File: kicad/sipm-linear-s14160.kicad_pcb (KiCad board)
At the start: 4 copper layers, 113.2 x 74.6 mm, 221 parts, among them J1 SSQ-103-01-G-D, J10 Conn_Coaxial, J11 Conn_Coaxial, J12 Conn_Coaxial, J13 Conn_Coaxial, J14 Conn_Coaxial, J15 Conn_Coaxial, J16 Conn_Coaxial, J17 Conn_Coaxial, J18 SSQ-103-01-G-D, J2 Conn_Coaxial, J3 Conn_Coaxial, J4 Conn_Coaxial, J5 Conn_Coaxial, J6 Conn_Coaxial, J7 Conn_Coaxial, J8 Conn_Coaxial, J9 Conn_Coaxial, U1 OPA847IDBVT, U10 OPA847IDBVT, U11 OPA847IDBVT, U12 OPA847IDBVT, U13 OPA847IDBVT, U14 OPA847IDBVT, U15 OPA847IDBVT, U16 OPA847IDBVT, U17 OPA847IDBVT, U2 S15643, U3 OPA847IDBVT, U4 OPA847IDBVT, U5 OPA847IDBVT, U6 OPA847IDBVT, U7 OPA847IDBVT, U8 OPA847IDBVT, U9 OPA847IDBVT

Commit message: Rename to reflect that we are using the s14160 elements in the array
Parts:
- moved J3 9.34 mm to (147.8, 77.2)
- moved J15 9.28 mm to (147.8, 130.8)
- moved J5 9.24 mm to (147.8, 87.9)
- moved J11 9.23 mm to (147.8, 120.1)
- moved J7 9.21 mm to (147.8, 98.6)
- moved J9 9.20 mm to (147.8, 109.4)
- moved J13 7.70 mm to (168.4, 74.6)
- moved C14 7.46 mm to (183.7, 104.2), turned to 0 degrees
- moved J18 6.58 mm to (178.4, 130.9)
- moved J17 6.05 mm to (168.2, 130.2)
- moved C40 5.16 mm to (183.7, 97.8), turned to 0 degrees
- moved J16 5.00 mm to (200.4, 130.4)
- moved L12 3.01 mm to (180.6, 89.8)
- moved J10 2.50 mm to (220.3, 119.1)
- moved J14 2.50 mm to (220.3, 108.6)
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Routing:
- added copper zone on In2.Cu, net /VBias2
- added copper zone on In2.Cu, net /VSSA2
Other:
- board size 113.2 x 74.6 mm -> 90.8 x 68.9 mm

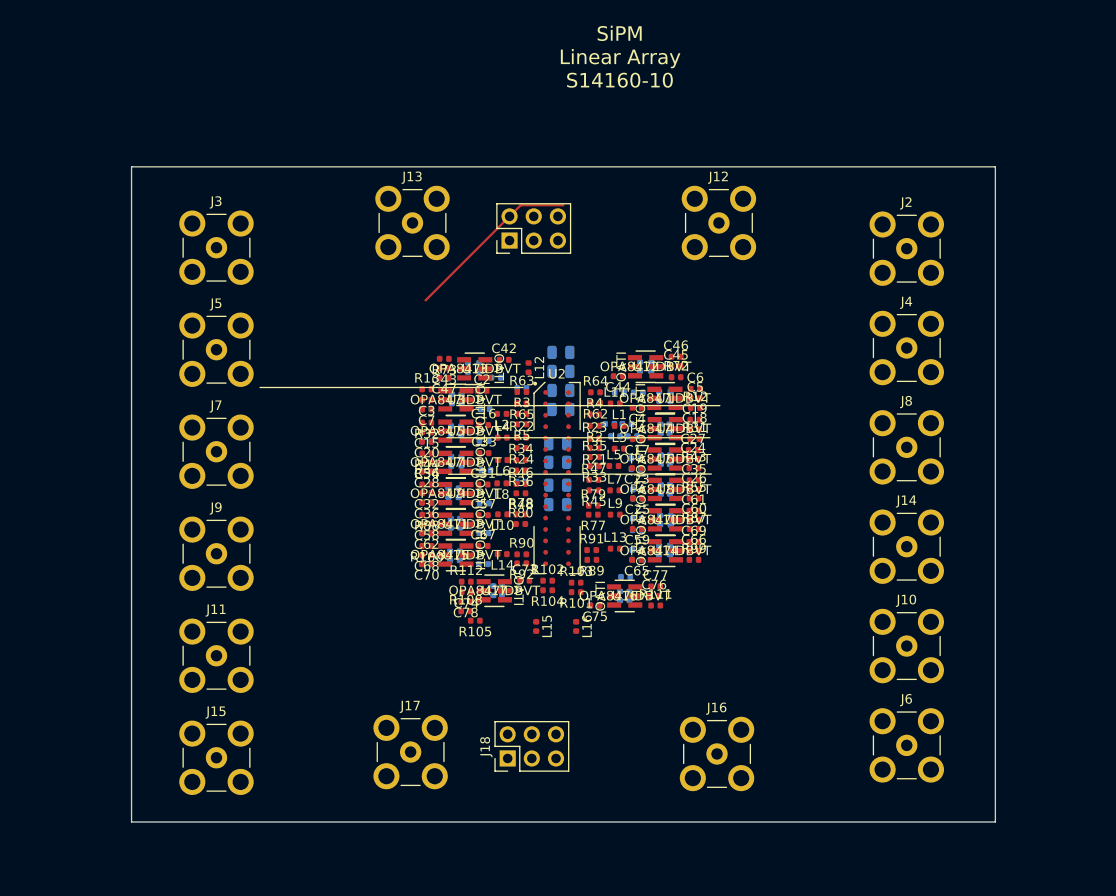
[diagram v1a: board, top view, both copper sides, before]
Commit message: Check in before removing feedback cap
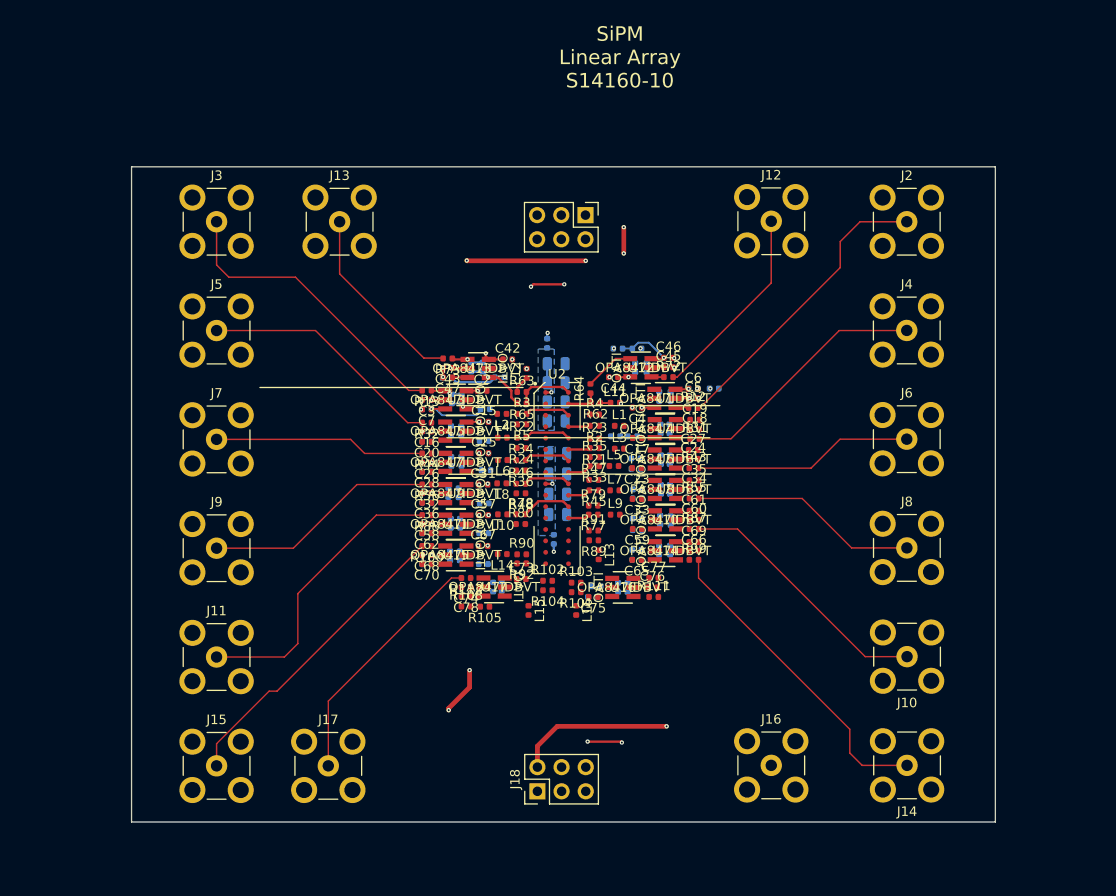
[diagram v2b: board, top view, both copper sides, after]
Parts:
- moved J6 32.2 mm to (220.3, 97.3)
- moved C34 28.2 mm to (198.0, 102.6), turned to 0 degrees
- moved C26 28.2 mm to (169.9, 99.8), turned to 180 degrees
- moved J14 23.0 mm to (220.4, 131.6), turned to 180 degrees
- moved C25 16.8 mm to (175.9, 98.8), turned to 0 degrees
- moved C33 16.8 mm to (192.0, 103.6), turned to 180 degrees
- moved J8 10.6 mm to (220.3, 108.7)
- moved R7 9.90 mm to (200.1, 92.0)
- moved R8 9.53 mm to (197.9, 92.0), turned to 180 degrees
- moved J17 8.77 mm to (159.6, 131.7)
- moved J1 8.41 mm to (186.6, 73.8), turned to -90 degrees
- moved J13 7.66 mm to (160.7, 74.5)
- moved R59 6.94 mm to (183.2, 107.8), turned to 90 degrees
- moved C15 6.10 mm to (175.9, 95.5), turned to 0 degrees
- moved C16 6.01 mm to (169.9, 96.5), turned to 180 degrees
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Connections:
- C31 pad 1: /VSSA2 -> /VDDA2
- C32 pad 1: /VDDA2 -> /VSSA2
- C33 pad 1: /VSSA2 -> /VDDA2
- C34 pad 1: /VDDA2 -> /VSSA2
- C57 pad 1: /VSSA2 -> /VDDA2
- C58 pad 1: /VDDA2 -> /VSSA2
- C59 pad 1: /VSSA2 -> /VDDA2
- C60 pad 1: /VDDA2 -> /VSSA2
- C65 pad 1: /VSSA2 -> /VDDA2
- C66 pad 1: /VDDA2 -> /VSSA2
- C67 pad 1: /VSSA2 -> /VDDA2
- C68 pad 1: /VDDA2 -> /VSSA2
- C73 pad 1: /VSSA2 -> /VDDA2
- C74 pad 1: /VDDA2 -> /VSSA2
- C75 pad 1: /VSSA2 -> /VDDA2
- C76 pad 1: /VDDA2 -> /VSSA2
- J1 pad 1: +5V -> unconnected-(J1-Pad1)
- J18 pad 1: +5V -> unconnected-(J18-Pad1)
- J18 pad 4: (no net) -> /LINE2
- R105 pad 1: LINE -> /LINE2
- R106 pad 2: LINE -> /LINE2
- R49 pad 1: LINE -> /LINE2
- R50 pad 2: LINE -> /LINE2
- R81 pad 1: LINE -> /LINE2
- R82 pad 2: LINE -> /LINE2
- R93 pad 1: LINE -> /LINE2
- R94 pad 2: LINE -> /LINE2
- U1 pad 5: (no net) -> unconnected-(U1-Pad5)
- U10 pad 2: /VDDA2 -> /VSSA2
- U10 pad 5: (no net) -> unconnected-(U10-Pad5)
- U10 pad 6: /VSSA2 -> /VDDA2
- U11 pad 2: /VDDA2 -> /VSSA2
- U11 pad 5: (no net) -> unconnected-(U11-Pad5)
- U11 pad 6: /VSSA2 -> /VDDA2
- U12 pad 5: (no net) -> unconnected-(U12-Pad5)
- U13 pad 5: (no net) -> unconnected-(U13-Pad5)
- U14 pad 2: /VDDA2 -> /VSSA2
- U14 pad 5: (no net) -> unconnected-(U14-Pad5)
- U14 pad 6: /VSSA2 -> /VDDA2
- U15 pad 2: /VDDA2 -> /VSSA2
- U15 pad 5: (no net) -> unconnected-(U15-Pad5)
- U15 pad 6: /VSSA2 -> /VDDA2
- U16 pad 2: /VDDA2 -> /VSSA2
- U16 pad 5: (no net) -> unconnected-(U16-Pad5)
- U16 pad 6: /VSSA2 -> /VDDA2
- U17 pad 2: /VDDA2 -> /VSSA2
- U17 pad 5: (no net) -> unconnected-(U17-Pad5)
- U17 pad 6: /VSSA2 -> /VDDA2
- U2 pad 11: (no net) -> unconnected-(U2-Pad11)
- U2 pad 13: (no net) -> unconnected-(U2-Pad13)
- U2 pad 15: (no net) -> unconnected-(U2-Pad15)
- U2 pad 19: (no net) -> unconnected-(U2-Pad19)
- U2 pad 21: (no net) -> unconnected-(U2-Pad21)
- U2 pad 23: (no net) -> unconnected-(U2-Pad23)
- U2 pad 25: (no net) -> unconnected-(U2-Pad25)
- U2 pad 27: (no net) -> unconnected-(U2-Pad27)
- U2 pad 29: (no net) -> unconnected-(U2-Pad29)
- U2 pad 3: (no net) -> unconnected-(U2-Pad3)
- U2 pad 31: (no net) -> unconnected-(U2-Pad31)
- U2 pad 5: (no net) -> unconnected-(U2-Pad5)
- U2 pad 7: (no net) -> unconnected-(U2-Pad7)
- U2 pad 9: (no net) -> unconnected-(U2-Pad9)
- U3 pad 5: (no net) -> unconnected-(U3-Pad5)
- U4 pad 5: (no net) -> unconnected-(U4-Pad5)
- U5 pad 5: (no net) -> unconnected-(U5-Pad5)
- U6 pad 5: (no net) -> unconnected-(U6-Pad5)
- U7 pad 5: (no net) -> unconnected-(U7-Pad5)
- U8 pad 2: /VDDA2 -> /VSSA2
- U8 pad 5: (no net) -> unconnected-(U8-Pad5)
- U8 pad 6: /VSSA2 -> /VDDA2
- U9 pad 2: /VDDA2 -> /VSSA2
- U9 pad 5: (no net) -> unconnected-(U9-Pad5)
- U9 pad 6: /VSSA2 -> /VDDA2
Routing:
- net /VDDA2: track 0.00 -> 67.8 mm, vias 0 -> 5
- net /VSSA2: track 0.00 -> 57.7 mm, vias 0 -> 4
- net /LINE2: track 0.00 -> 46.6 mm, vias 0 -> 2
- net GND: track 34.6 -> 1.00 mm, vias 0 -> 24
- net Net-(J14-Pad1): track 0.00 -> 33.4 mm
- net Net-(J15-Pad1): track 0.00 -> 32.5 mm
- net Net-(J2-Pad1): track 0.00 -> 31.7 mm
- net Net-(J3-Pad1): track 0.00 -> 31.6 mm
- net Net-(J11-Pad1): track 0.00 -> 30.9 mm
- net VDDA: track 20.0 -> 49.6 mm, vias 0 -> 8
- net VSSA: track 18.6 -> 46.7 mm, vias 0 -> 7
- net Net-(J10-Pad1): track 0.00 -> 27.4 mm
- net Net-(J4-Pad1): track 0.00 -> 26.5 mm
- net Net-(J17-Pad1): track 0.00 -> 26.1 mm
- net Net-(J5-Pad1): track 0.00 -> 25.6 mm
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- added copper zone on In2.Cu, net /LINE2
- added copper zone on In2.Cu, net /VBias
- added copper zone on In2.Cu, net /VDDA2
- added copper zone on B.Cu, net Net-(C1-Pad1)
- added copper zone on B.Cu, net Net-(C14-Pad1)
- removed copper zone on In2.Cu, net (none)

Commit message: First version that passes schematic parity check
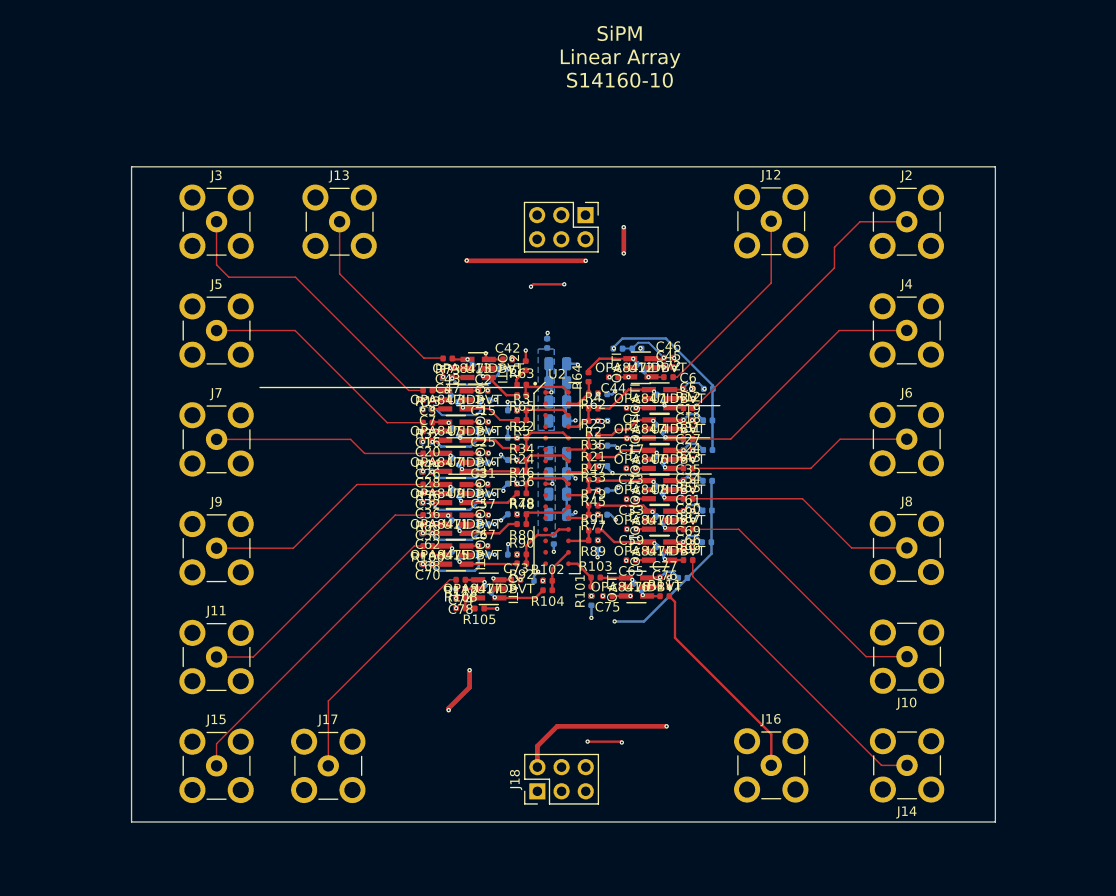
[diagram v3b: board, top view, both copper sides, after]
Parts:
- removed C21, C22, C29, C30, C37, C38, C48, C49, C63, C64, C71, C72, C79, C8, C80, C9: 1p, Capacitor_SMD:C_0402_1005Metric
- L1, L10, L11, L13, L14, L15, L16, L2, L3, L4, L5, L6, L7, L8, L9: moved to B.Cu
- moved R26 9.85 mm to (199.4, 95.4), turned to 0 degrees
- moved R106 9.69 mm to (196.8, 111.9), turned to 0 degrees
- moved R38 7.62 mm to (199.4, 98.5), turned to 0 degrees
- moved R94 7.57 mm to (199.3, 108.2)
- moved R50 7.41 mm to (199.4, 101.7), turned to 0 degrees
- moved R82 7.40 mm to (199.4, 104.8), turned to 0 degrees
- moved R107 7.25 mm to (194.9, 111.9), turned to 180 degrees
- moved L15 6.68 mm to (187.2, 114.3)
- moved R27 6.09 mm to (197.4, 95.3)
- moved R39 5.83 mm to (197.4, 98.5), turned to 180 degrees
- moved R83 5.71 mm to (197.4, 104.9), turned to 180 degrees
- moved R51 5.64 mm to (197.4, 101.7), turned to 180 degrees
- moved R95 5.44 mm to (197.4, 108.2), turned to 180 degrees
- moved L16 5.03 mm to (181.7, 112.2), turned to 180 degrees
- moved R103 2.12 mm to (187.7, 111.9)
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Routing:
- net GND: track 1.00 -> 36.3 mm, vias 24 -> 70
- net Net-(J16-Pad1): track 0.00 -> 22.2 mm
- net LINE: track 22.4 -> 44.2 mm, vias 4 -> 7
- net /LINE2: track 46.6 -> 64.1 mm, vias 2 -> 7
- net /VSSA2: track 57.7 -> 69.5 mm, vias 4 -> 9
- net Net-(C70-Pad1): track 0.00 -> 8.08 mm, vias 0 -> 1
- net Net-(C28-Pad1): track 0.00 -> 7.98 mm, vias 0 -> 1
- net Net-(C62-Pad1): track 0.00 -> 7.85 mm, vias 0 -> 1
- net Net-(C36-Pad1): track 0.00 -> 7.83 mm, vias 0 -> 1
- net Net-(C20-Pad1): track 0.00 -> 7.61 mm, vias 0 -> 1
- net Net-(R10-Pad1): track 0.00 -> 7.32 mm, vias 0 -> 1
- net Net-(R23-Pad2): track 0.00 -> 7.08 mm, vias 0 -> 1
- net /SipmPair6/IN1: track 0.00 -> 6.98 mm
- net Net-(R91-Pad2): track 0.00 -> 6.98 mm, vias 0 -> 1
- net VSSA: track 46.7 -> 53.7 mm, vias 7 -> 10
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
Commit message: Near final version
Sorted out the line input, flipped the connectors around to the correct board side and cleaned up the silkscreen.
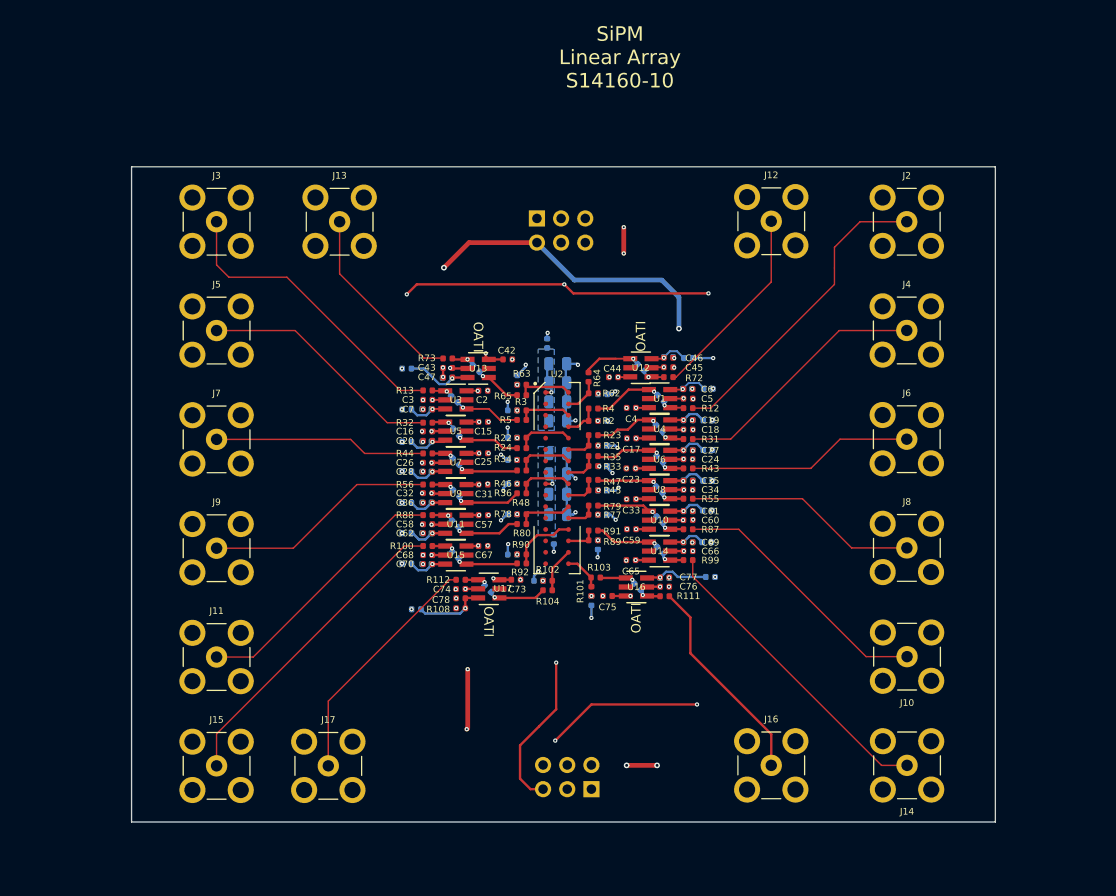
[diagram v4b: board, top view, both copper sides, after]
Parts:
- J1, J18, L12, R105: moved to B.Cu
- moved R14 10.1 mm to (167.8, 89.9), turned to 0 degrees
- moved R6 8.28 mm to (167.8, 94.2), turned to 0 degrees
- moved R81 8.11 mm to (167.8, 107.2), turned to 0 degrees
- moved R93 8.11 mm to (167.8, 110.4), turned to 0 degrees
- moved R25 8.08 mm to (167.8, 97.6), turned to 0 degrees
- moved R49 8.06 mm to (167.8, 104.0), turned to 0 degrees
- moved R37 8.03 mm to (167.8, 100.7), turned to 0 degrees
- moved R15 7.48 mm to (197.4, 88.8), turned to 0 degrees
- moved R105 6.64 mm to (168.8, 115.2), turned to 0 degrees
- moved J18 5.68 mm to (187.2, 134.1)
- moved J1 5.11 mm to (181.5, 74.1)
- moved R68 3.43 mm to (195.3, 88.7)
- moved R106 2.90 mm to (199.7, 111.8)
- moved L12 1.75 mm to (179.4, 91.1)
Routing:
- net /LINE2: track 64.1 -> 55.1 mm, vias 7 -> 10
- net /VSSA2: track 69.5 -> 62.4 mm, vias 9 -> 10
- net Net-(C7-Pad1): track 8.18 -> 4.14 mm
- net Net-(C62-Pad1): track 7.85 -> 3.82 mm
- net Net-(C78-Pad1): track 3.43 -> 7.43 mm, vias 0 -> 1
- net Net-(C70-Pad1): track 8.08 -> 4.11 mm
- net Net-(C28-Pad1): track 7.98 -> 4.06 mm
- net Net-(C36-Pad1): track 7.83 -> 3.96 mm
- net LINE: track 44.2 -> 48.0 mm, vias 7 -> 11
- net Net-(C20-Pad1): track 7.61 -> 4.13 mm
- net /VDDA2: track 70.2 -> 67.0 mm
- net VSSA: track 53.7 -> 50.6 mm
- net GND: track 36.3 -> 33.5 mm, vias 70 -> 69
- net Net-(C46-Pad1): track 6.60 -> 3.86 mm
- net Net-(C77-Pad1): track 3.87 -> 6.60 mm
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
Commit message: Update the PCB with final PZC and offset values
In testing, the PZC worked well with 6.3/43/90nH on the S14160-1315 which we are assuming is very similar.  These values may not be quite right for the array but are hopefully close.  The 68/5000 ohm offset divider also seemed optimal on the single sipm.
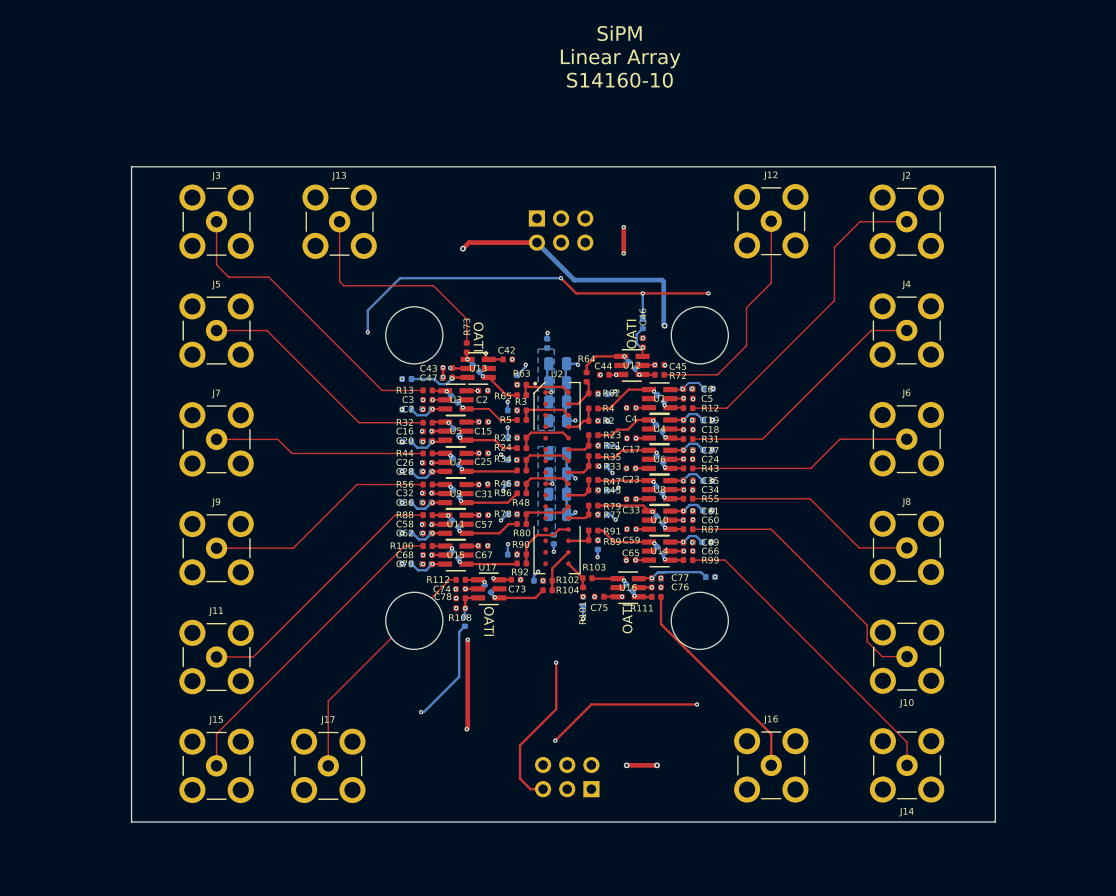
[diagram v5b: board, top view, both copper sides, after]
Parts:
- added H1: MountingHole, MountingHole:MountingHole_6mm, F.Cu at (198.6, 86.4)
- added H2: MountingHole, MountingHole:MountingHole_6mm, F.Cu at (168.6, 116.4)
- added H3: MountingHole, MountingHole:MountingHole_6mm, F.Cu at (168.6, 86.4)
- added H4: MountingHole, MountingHole:MountingHole_6mm, F.Cu at (198.6, 116.4)
- L1, L10, L11, L12, L13, L14, L15, L16, L2, L3, L4, L5, L6, L7, L8, L9: value 0.033uH -> 0.090uH
- R101, R102, R2, R21, R22, R3, R33, R34, R45, R46, R62, R63, R77, R78, R89, R90: value 3.3 -> 6.3
- R103, R104, R23, R24, R35, R36, R4, R47, R48, R5, R64, R65, R79, R80, R91, R92: value 33 -> 43
- R107, R108, R27, R28, R39, R40, R51, R52, R68, R69, R8, R83, R84, R9, R95, R96: value 5000 -> 68
- moved R15 6.00 mm to (192.6, 85.2), turned to 90 degrees
- moved R105 5.26 mm to (173.9, 116.5), turned to 90 degrees
- moved C46 3.13 mm to (192.6, 87.2), turned to 90 degrees
- moved R68 3.09 mm to (192.6, 87.2), turned to -90 degrees
- moved R73 2.30 mm to (174.1, 87.7), turned to 90 degrees
- moved R14 1.10 mm to (167.8, 91.0)
- moved C44 0.97 mm to (188.6, 90.6)
- moved C45 0.97 mm to (194.4, 89.5)
- moved R70 0.97 mm to (191.5, 89.6)
- moved R72 0.97 mm to (194.4, 90.6)
- moved U12 0.97 mm to (191.5, 89.6)
- moved C75 0.87 mm to (188.0, 113.9)
- moved C76 0.87 mm to (194.0, 112.9)
- moved C77 0.87 mm to (194.0, 111.9)
- moved L15 0.87 mm to (186.3, 114.4)
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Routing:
- net /LINE2: track 55.1 -> 83.2 mm
- net LINE: track 48.0 -> 69.3 mm
- net Net-(C78-Pad1): track 7.43 -> 3.39 mm
- net Net-(J13-Pad1): track 20.0 -> 23.8 mm
- net Net-(J12-Pad1): track 20.8 -> 24.1 mm
- net /VSSA2: track 62.4 -> 61.3 mm
- net Net-(C77-Pad1): track 6.60 -> 7.61 mm
- net Net-(J2-Pad1): track 33.0 -> 34.0 mm
- net Net-(J10-Pad1): track 28.0 -> 29.0 mm
- net /SipmPair7/IN2: track 4.12 -> 3.19 mm
- net Net-(R71-Pad2): track 2.31 -> 1.49 mm
- net Net-(R64-Pad2): track 6.27 -> 5.54 mm
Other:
- board text added: "CH0"
- board text added: "CH1"
- board text added: "CH10"
- board text added: "CH11"
- board text added: "CH12"
- board text added: "CH13"
- board text added: "CH2"
- board text added: "CH3"
- board text added: "CH4"
- board text added: "CH5"
- board text added: "CH6"
- board text added: "CH7"
- board text added: "CH8"
- board text added: "CH9"
- board text added: "SIPM Linear S14420 Custom Array V1.0"
